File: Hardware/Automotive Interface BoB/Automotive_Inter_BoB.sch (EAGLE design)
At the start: 31 parts, among them U1 HCPL-270L

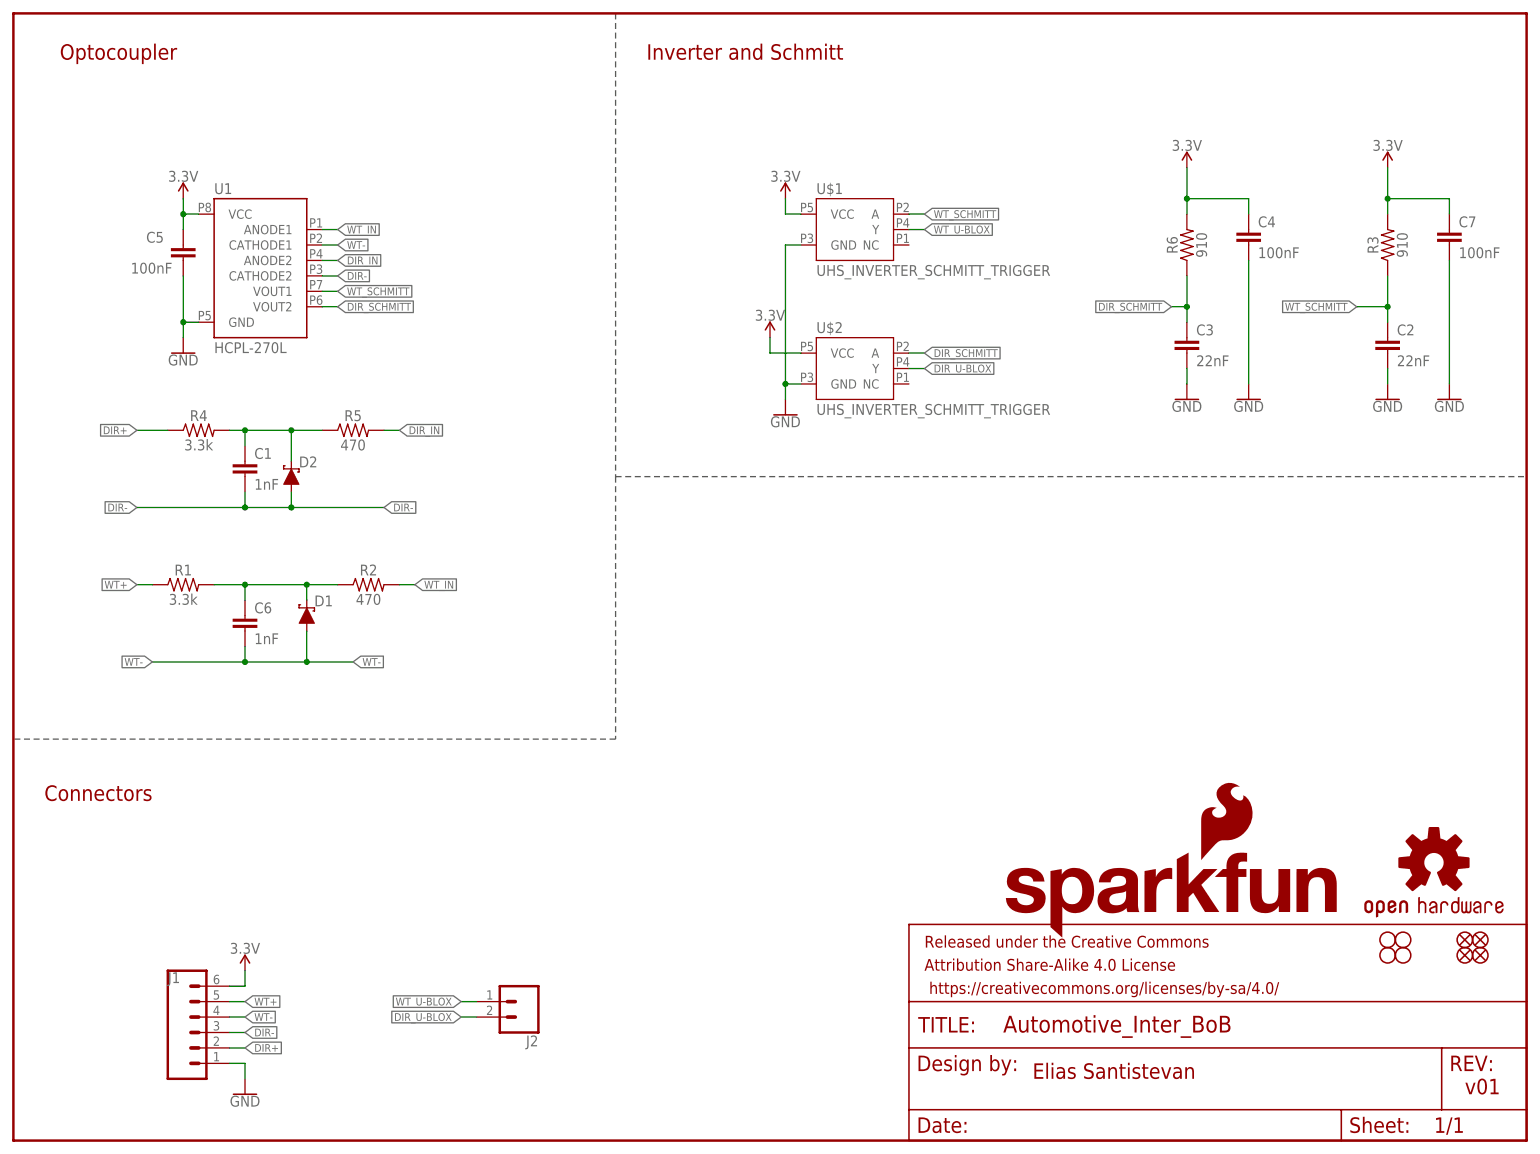
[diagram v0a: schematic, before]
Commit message: Updates the optocoupler in the Automotive breakout
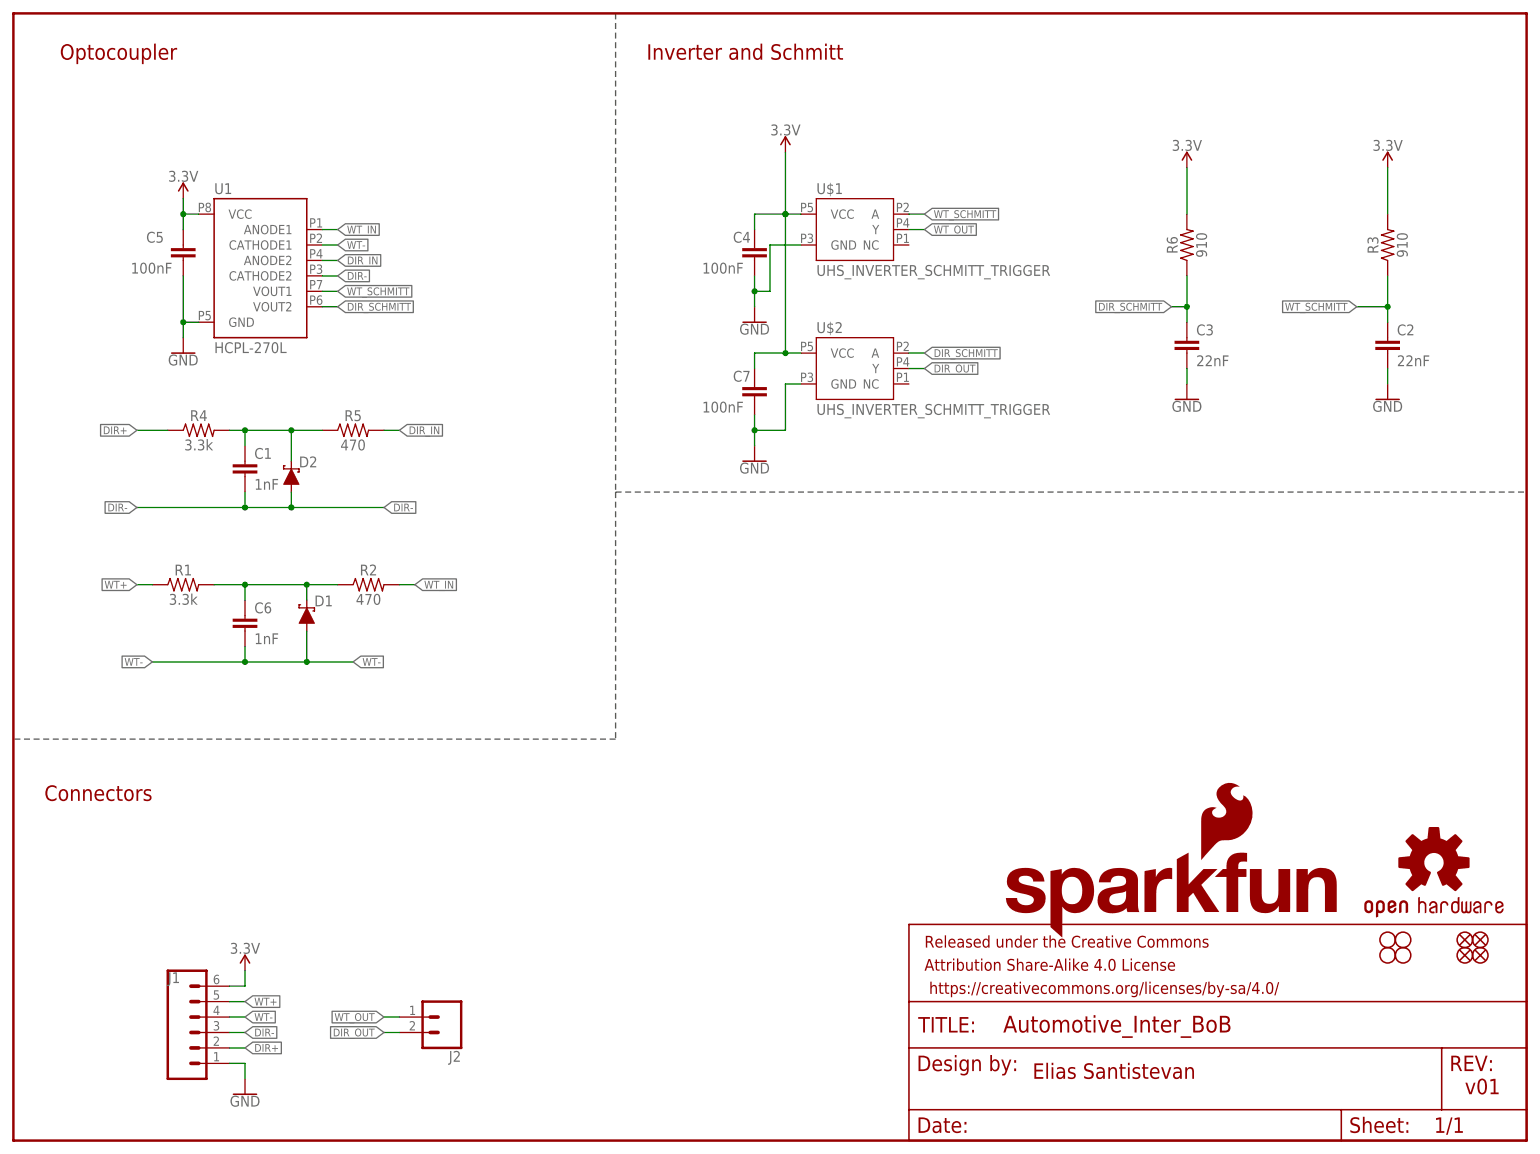
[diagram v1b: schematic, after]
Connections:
- net DIR_U-BLOX renamed DIR_OUT
- net WT_U-BLOX renamed WT_OUT
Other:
- moved on the sheet: C4, C7, J2
